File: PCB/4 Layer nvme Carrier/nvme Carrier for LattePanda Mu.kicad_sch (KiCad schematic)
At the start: 8 parts

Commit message: Prototyp_1
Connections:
- no-connect marks 2 -> 1
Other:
- sheet LattePanda Module ports: added TSENSE; removed none
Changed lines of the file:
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@@
 	)
 	(no_connect
-		(at 167.64 140.97)
-	)
-	(no_connect
 		(at 367.03 114.3)
 	)
@@
 	(wire
 		(pts
+			(xy 195.58 129.54) (xy 227.33 129.54)
+		)
+		(stroke
+			(width 0)
+			(type default)
+		)
+	)
+	(wire
+		(pts
 			(xy 367.03 160.02) (xy 341.63 160.02)
 		)
@@
 		(unit 1)
 		(exclude_from_sim no)
-		(in_bom yes)
+		(in_bom no)
 		(on_board yes)
 		(dnp no)
@@
 		(unit 1)
 		(exclude_from_sim no)
-		(in_bom yes)
+		(in_bom no)
 		(on_board yes)
 		(dnp no)
@@
 		(unit 1)
 		(exclude_from_sim no)
-		(in_bom yes)
+		(in_bom no)
 		(on_board yes)
 		(dnp no)
@@
 		(unit 1)
 		(exclude_from_sim no)
-		(in_bom yes)
+		(in_bom no)
 		(on_board yes)
 		(dnp no)
@@
 		(unit 1)
 		(exclude_from_sim no)
-		(in_bom yes)
+		(in_bom no)
 		(on_board yes)
 		(dnp no)
@@
 		(unit 1)
 		(exclude_from_sim no)
-		(in_bom yes)
+		(in_bom no)
 		(on_board yes)
 		(dnp no)
@@
 		(unit 1)
 		(exclude_from_sim no)
-		(in_bom yes)
+		(in_bom no)
 		(on_board yes)
 		(dnp no)
@@
 		(unit 1)
 		(exclude_from_sim no)
-		(in_bom yes)
+		(in_bom no)
 		(on_board yes)
 		(dnp no)
@@
 	)
 	(sheet
-		(at 167.64 129.54)
-		(size 27.94 17.78)
+		(at 167.64 127)
+		(size 27.94 20.32)
 		(fields_autoplaced yes)
 		(stroke
@@
 		)
 		(property "Sheetname" "Fan_Temp"
-			(at 167.64 128.8284 0)
+			(at 167.64 126.2884 0)
 			(effects
 				(font
@@
 		)
 		(pin "TEMP" output
-			(at 167.64 140.97 180)
+			(at 195.58 129.54 0)
 			(effects
 				(font
 					(size 1.27 1.27)
 				)
-				(justify left)
+				(justify right)
 			)
 		)
@@
 			(effects
 				(font
+					(size 1.27 1.27)
+				)
+				(justify left)
+			)
+		)
+		(pin "TSENSE" input
+			(at 227.33 129.54 180)
+			(effects
+				(font

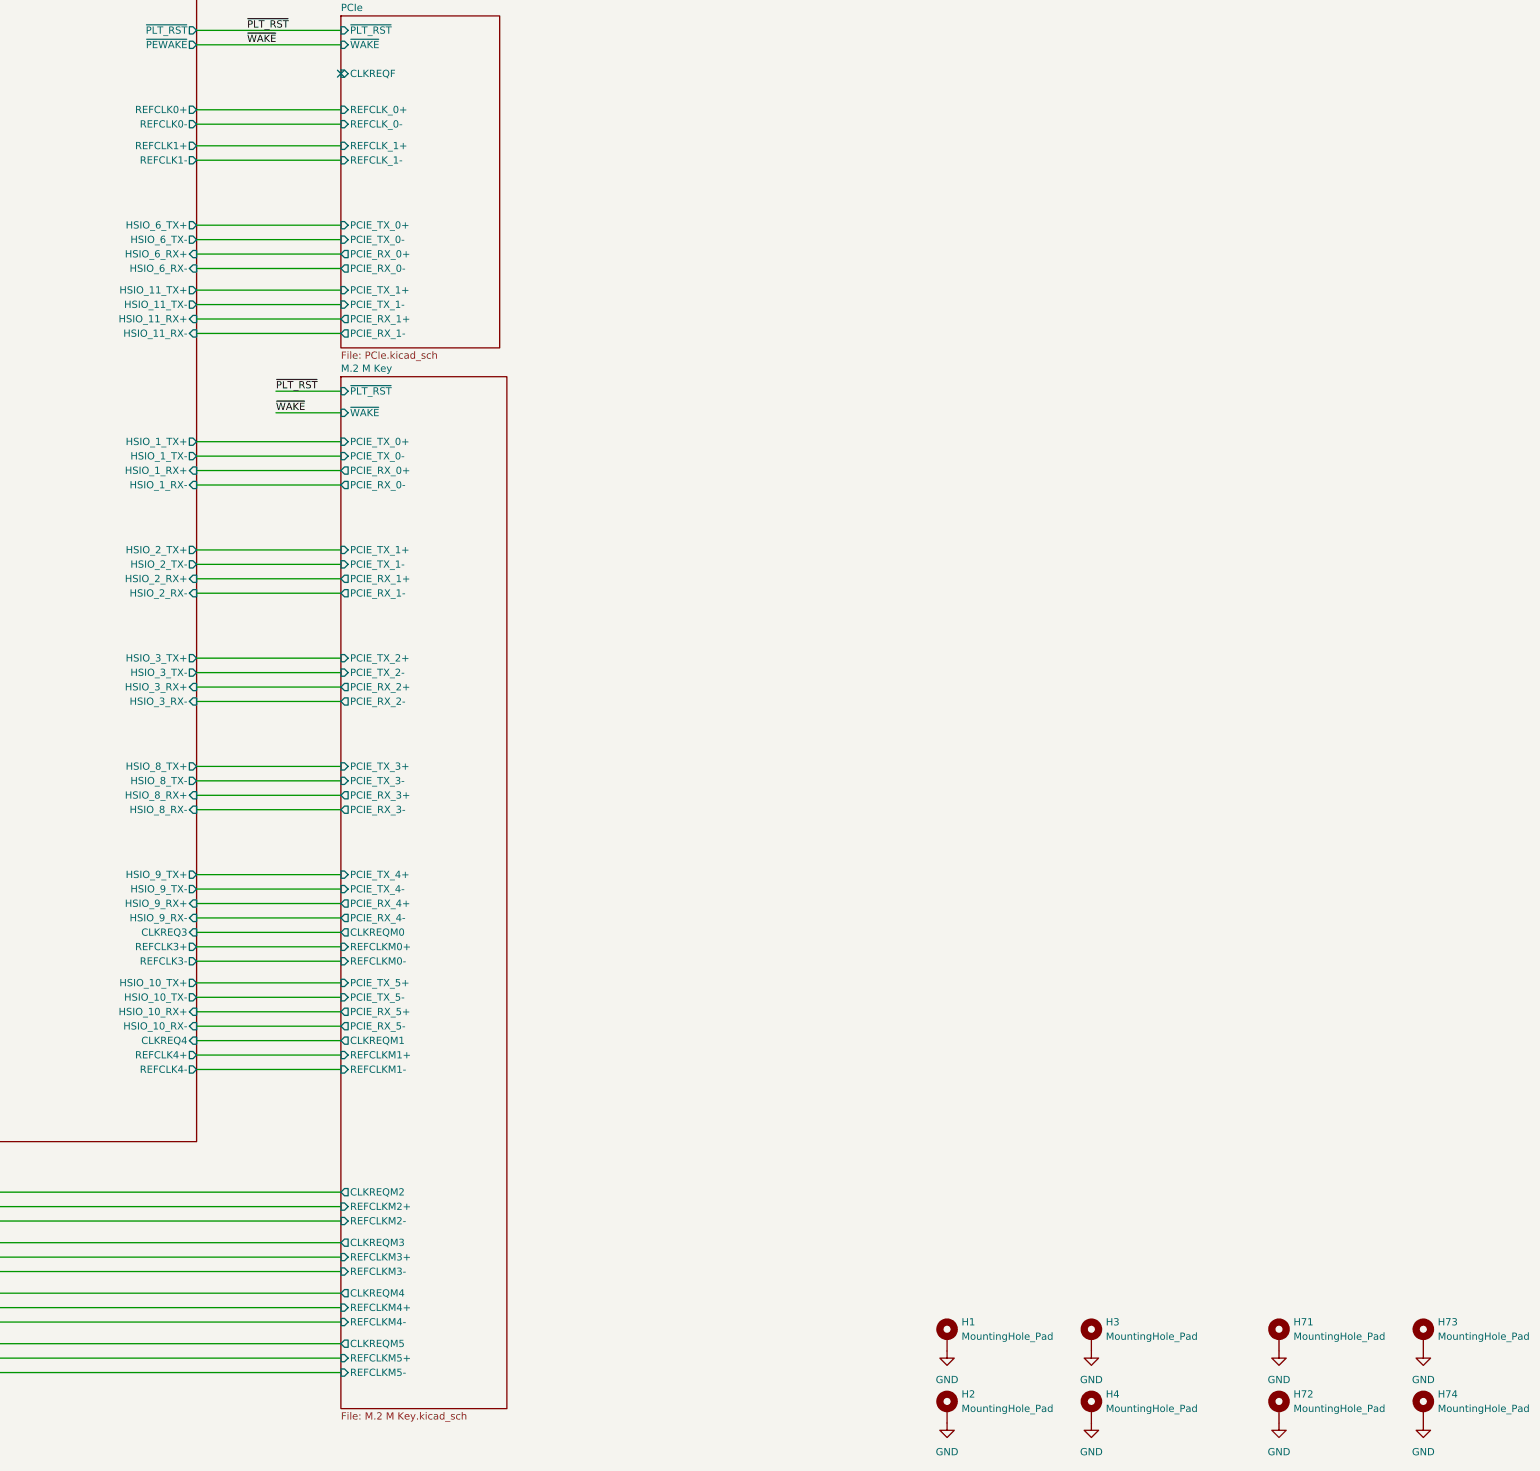
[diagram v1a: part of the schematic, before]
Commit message: Silk and BOM changes
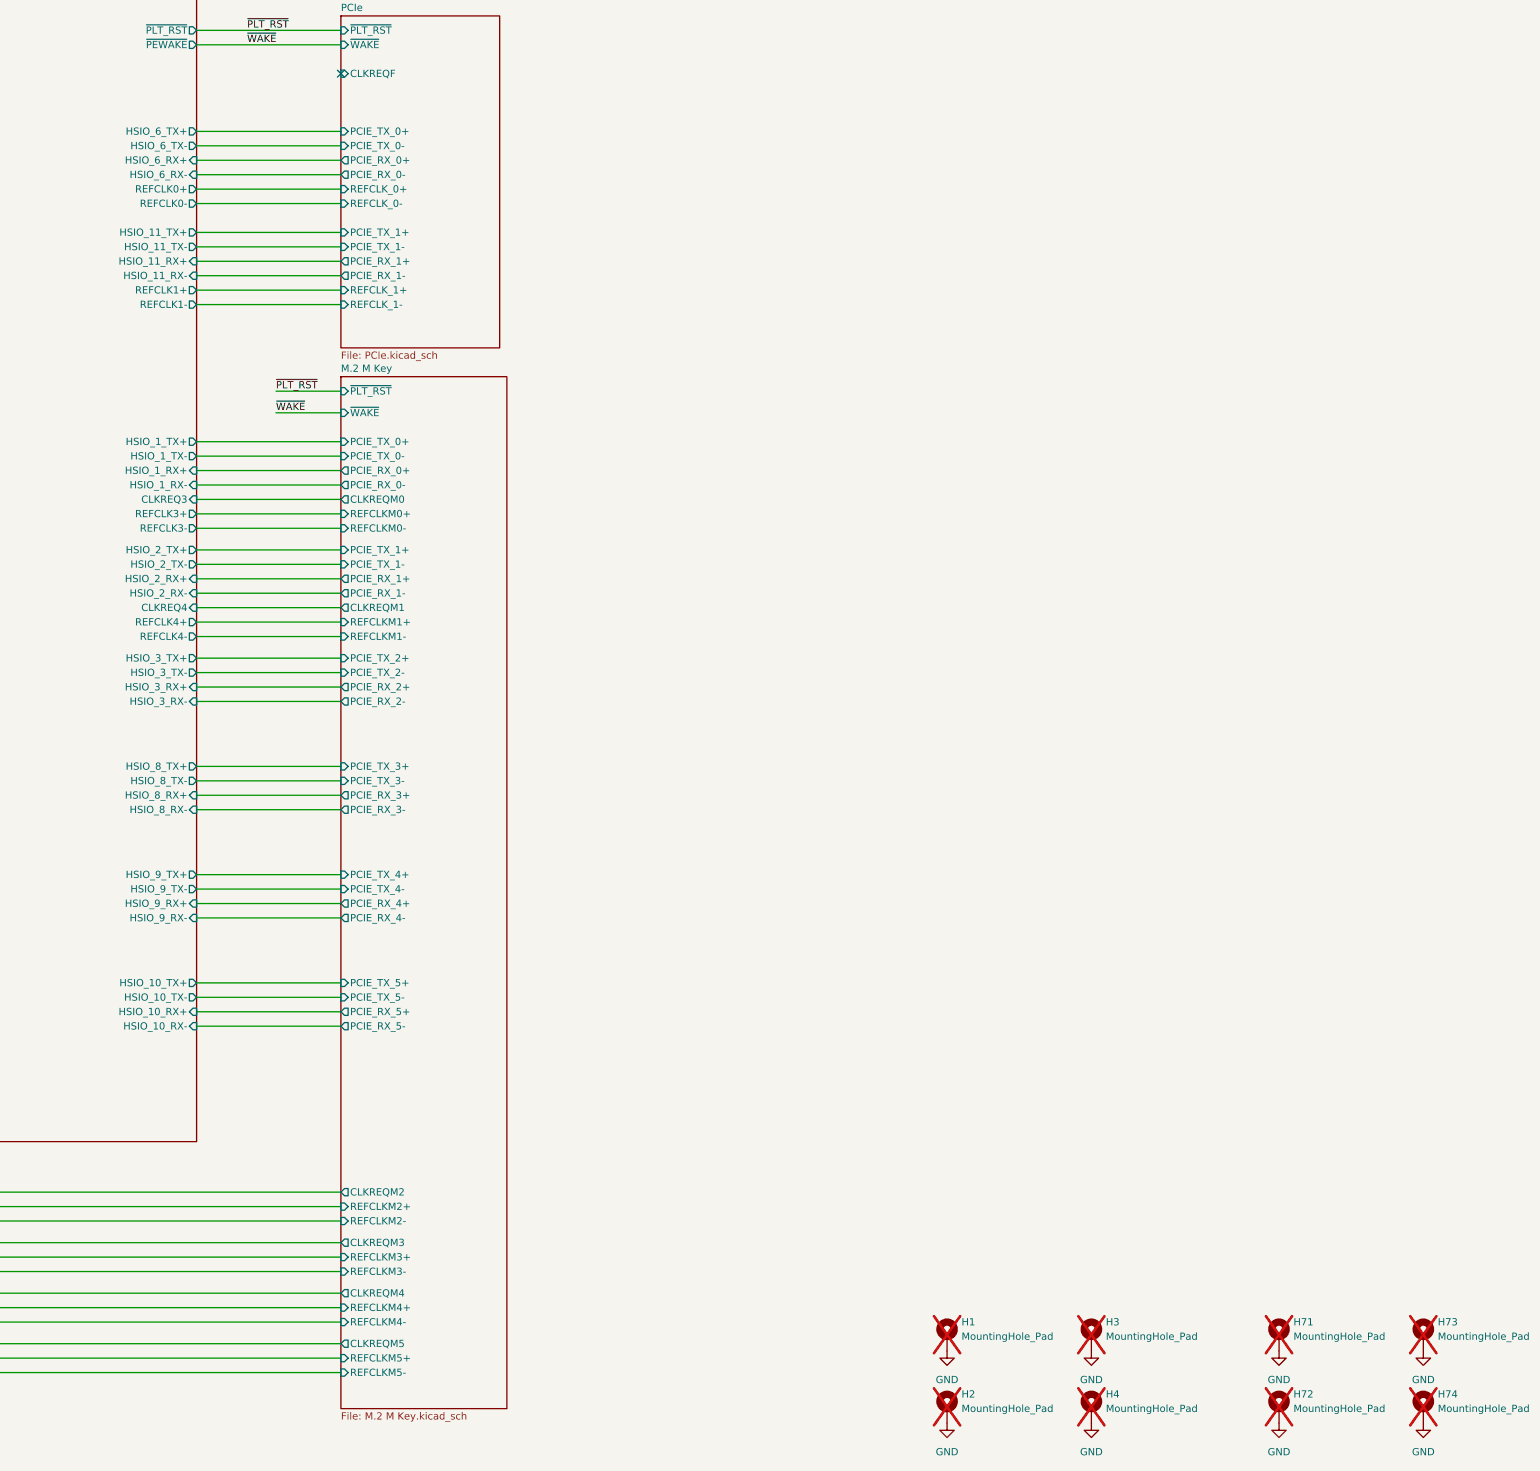
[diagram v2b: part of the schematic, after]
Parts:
- H1, H2, H3, H4, H71, H72, H73, H74: now not fitted
